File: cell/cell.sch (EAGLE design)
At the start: 11 parts

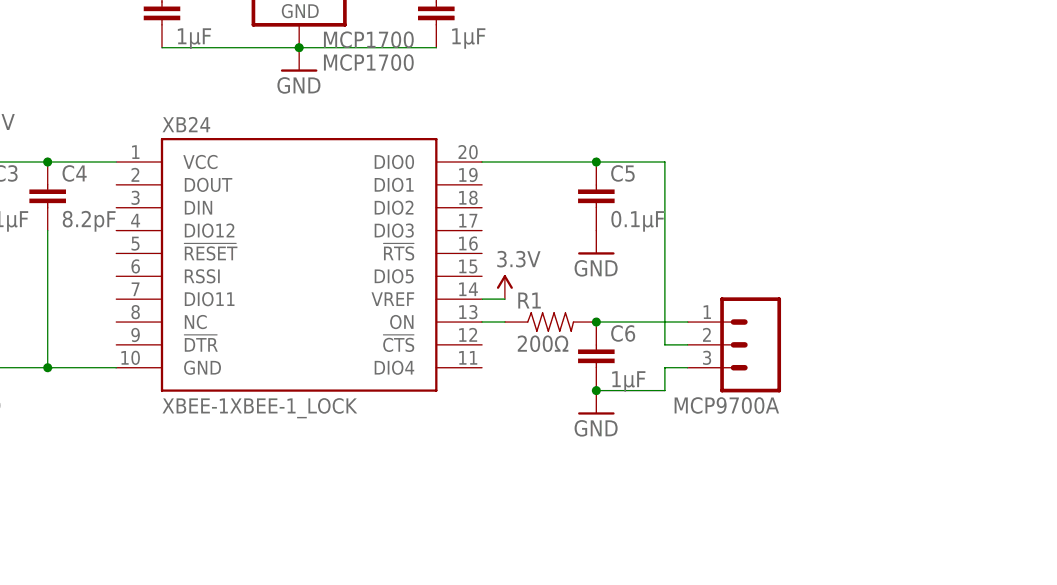
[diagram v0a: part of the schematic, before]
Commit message: cell v0.2, with on-board temperature sensor and better layout
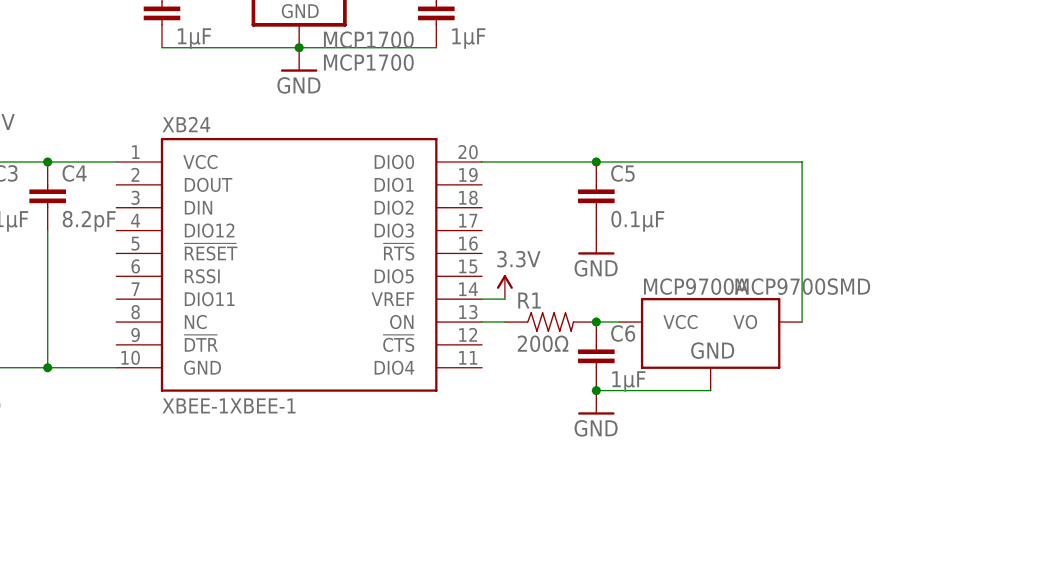
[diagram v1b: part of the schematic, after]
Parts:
- MCP9700A: value (none) -> MCP9700SMD; device SparkFun-Connectors:M03LOCK -> SparkFun-Sensors:MCP9700SMD
- XB24: value XBEE-1XBEE-1_LOCK -> XBEE-1XBEE-1; device hrldcpr:XBEE-1XBEE-1_LOCK -> hrldcpr:XBEE-1XBEE-1
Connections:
- net GND: now also MCP9700A.GND; no longer MCP9700A.3
- net N$1: now also MCP9700A.VCC; no longer MCP9700A.1
- net N$3: now also MCP9700A.VO; no longer MCP9700A.2
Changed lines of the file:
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@@
 <part name="C6" library="SparkFun-Capacitors" deviceset="CAP" device="0805" value="1µF"/>
 <part name="R1" library="SparkFun-Resistors" deviceset="RESISTOR" device="0805-RES" value="200Ω"/>
-<part name="XB24" library="hrldcpr" deviceset="XBEE-1" device="XBEE-1_LOCK"/>
 <part name="MCP1700" library="hrldcpr" deviceset="MCP1700" device=""/>
 <part name="C2" library="SparkFun-Capacitors" deviceset="CAP" device="0805" value="1µF"/>
-<part name="MCP9700A" library="SparkFun-Connectors" deviceset="M03" device="LOCK"/>
+<part name="MCP9700A" library="SparkFun-Sensors" deviceset="MCP9700" device="SMD"/>
+<part name="XB24" library="hrldcpr" deviceset="XBEE-1" device="XBEE-1"/>
 </parts>
 <sheets>
@@
 <instance part="C6" gate="G$1" x="137.16" y="76.2"/>
 <instance part="R1" gate="G$1" x="132.08" y="81.28"/>
-<instance part="XB24" gate="G$1" x="104.14" y="88.9"/>
 <instance part="MCP1700" gate="G$1" x="104.14" y="119.38"/>
 <instance part="C2" gate="G$1" x="119.38" y="114.3"/>
-<instance part="MCP9700A" gate="G$1" x="154.94" y="78.74" rot="R180"/>
+<instance part="MCP9700A" gate="G$1" x="149.86" y="78.74"/>
+<instance part="XB24" gate="G$1" x="104.14" y="88.9"/>
 </instances>
 <busses>
@@
 <pinref part="C6" gate="G$1" pin="2"/>
 <pinref part="C6" gate="G$1" pin="2"/>
-<wire x1="144.78" y1="76.2" x2="144.78" y2="73.66" width="0.1524" layer="91"/>
-<wire x1="144.78" y1="73.66" x2="137.16" y2="73.66" width="0.1524" layer="91"/>
 <junction x="137.16" y="73.66"/>
-<pinref part="MCP9700A" gate="G$1" pin="3"/>
-<wire x1="144.78" y1="76.2" x2="147.32" y2="76.2" width="0.1524" layer="91"/>
+<pinref part="MCP9700A" gate="G$1" pin="GND"/>
+<wire x1="137.16" y1="73.66" x2="149.86" y2="73.66" width="0.1524" layer="91"/>
 </segment>
 <segment>
@@
 <pinref part="C6" gate="G$1" pin="1"/>
 <pinref part="R1" gate="G$1" pin="2"/>
-<wire x1="147.32" y1="81.28" x2="137.16" y2="81.28" width="0.1524" layer="91"/>
+<pinref part="MCP9700A" gate="G$1" pin="VCC"/>
+<pinref part="MCP9700A" gate="G$1" pin="VCC"/>
+<wire x1="139.7" y1="81.28" x2="137.16" y2="81.28" width="0.1524" layer="91"/>
 <junction x="137.16" y="81.28"/>
-<pinref part="MCP9700A" gate="G$1" pin="1"/>
 </segment>
 </net>
@@
 <pinref part="C5" gate="G$1" pin="1"/>
 <wire x1="137.16" y1="99.06" x2="124.46" y2="99.06" width="0.1524" layer="91"/>
-<wire x1="137.16" y1="99.06" x2="144.78" y2="99.06" width="0.1524" layer="91"/>
-<wire x1="144.78" y1="99.06" x2="144.78" y2="78.74" width="0.1524" layer="91"/>
 <junction x="137.16" y="99.06"/>
+<pinref part="MCP9700A" gate="G$1" pin="VO"/>
+<wire x1="160.02" y1="81.28" x2="160.02" y2="99.06" width="0.1524" layer="91"/>
+<wire x1="160.02" y1="99.06" x2="137.16" y2="99.06" width="0.1524" layer="91"/>
 <pinref part="XB24" gate="G$1" pin="DIO0"/>
-<pinref part="MCP9700A" gate="G$1" pin="2"/>
-<wire x1="144.78" y1="78.74" x2="147.32" y2="78.74" width="0.1524" layer="91"/>
 </segment>
 </net>

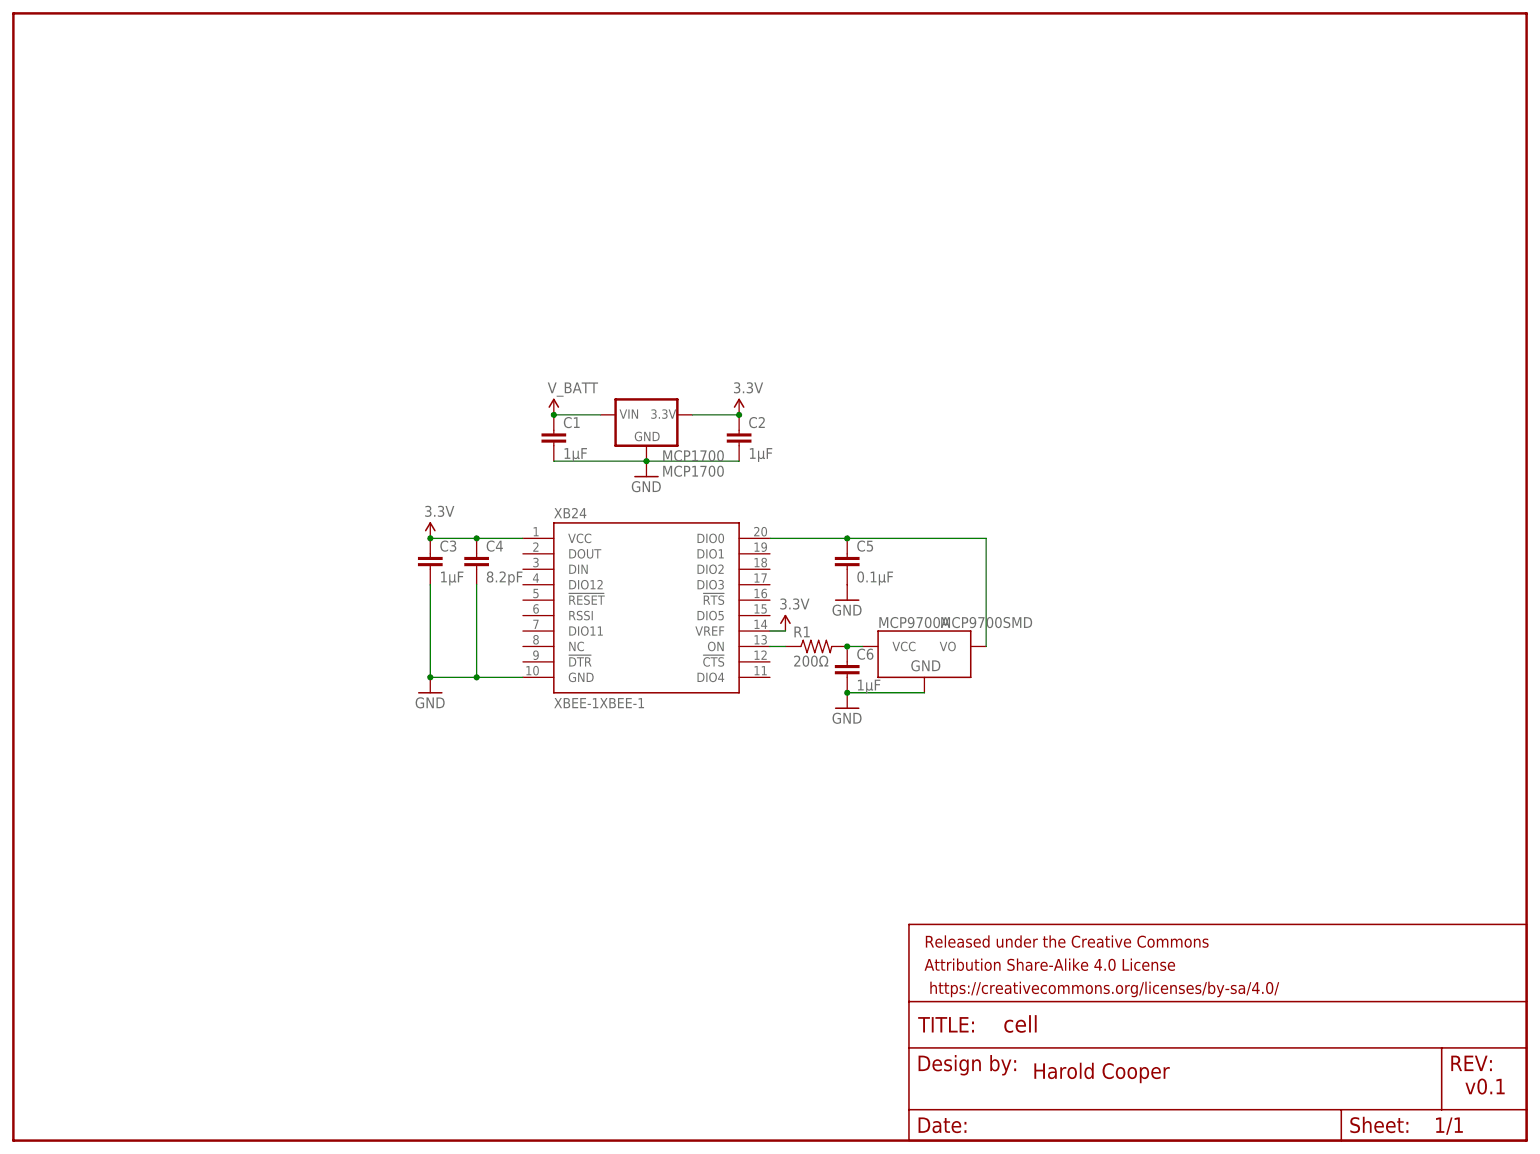
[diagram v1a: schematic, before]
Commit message: ground DIN/!CONFIG so that we can safely disable its pullup resistor
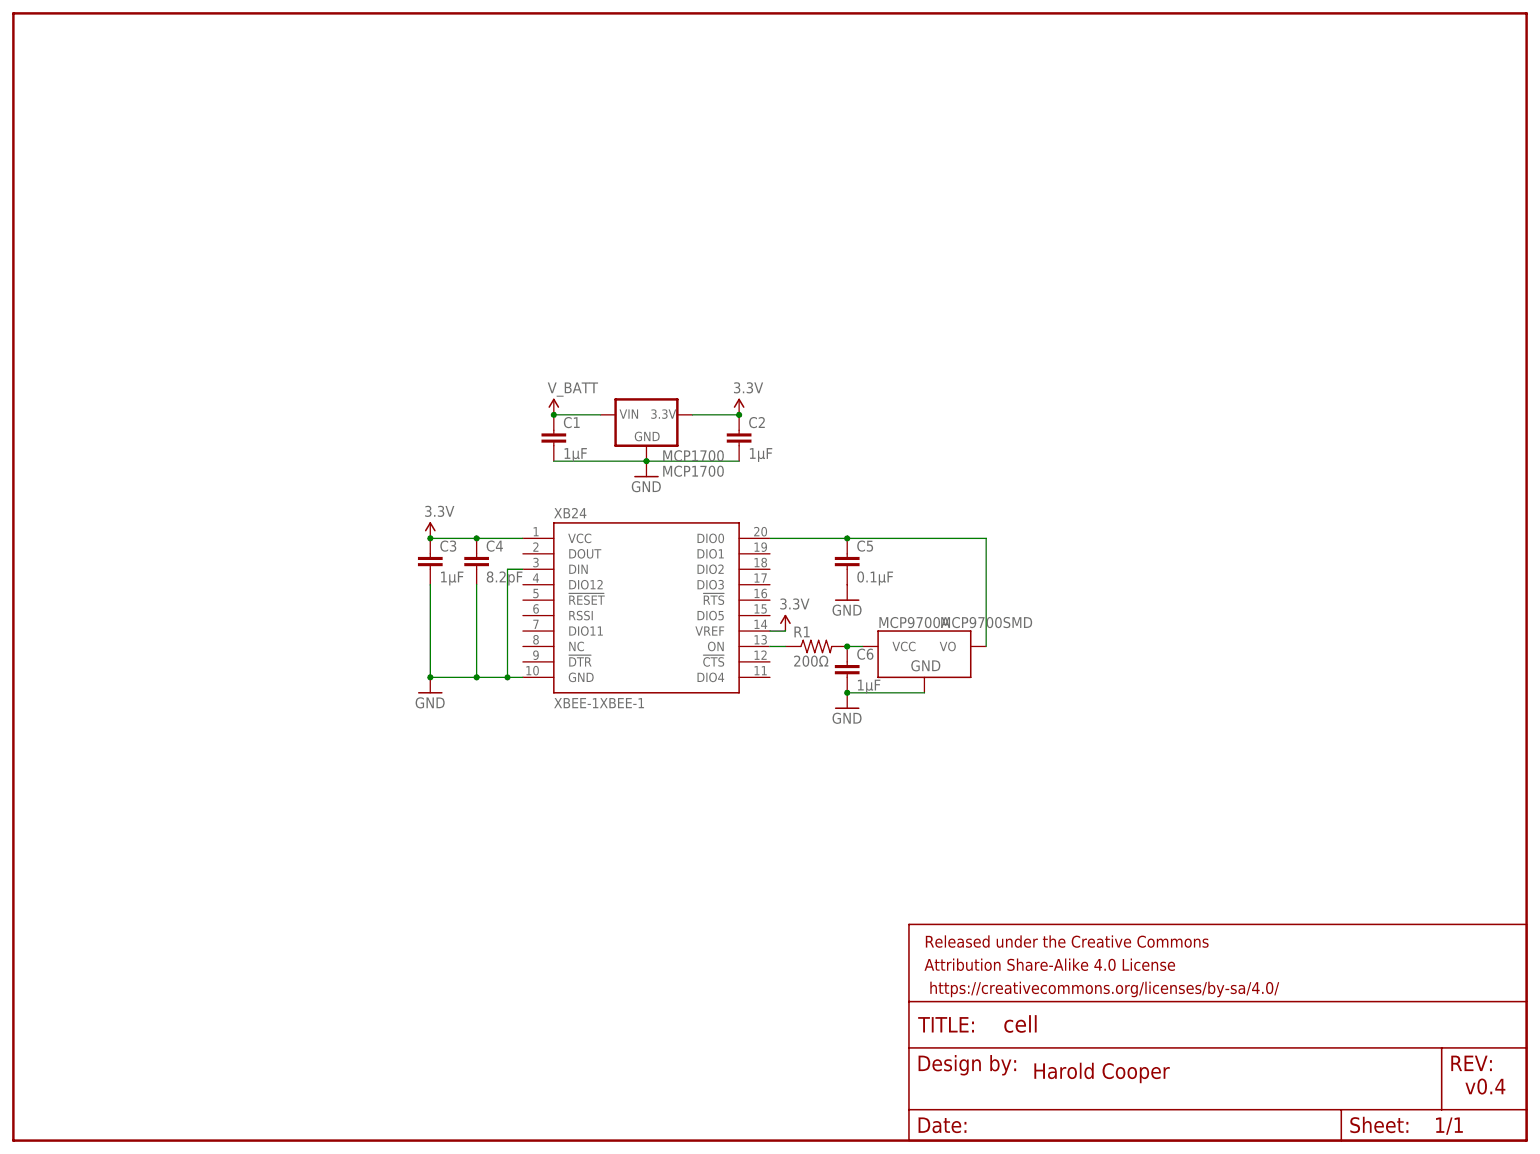
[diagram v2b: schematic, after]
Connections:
- net GND: now also XB24.DIN
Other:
- note added: "v0.4"
- note removed: "v0.1"
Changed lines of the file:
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@@
 <plain>
 <text x="167.64" y="10.16" size="2.54" layer="94">Harold Cooper</text>
-<text x="238.76" y="7.62" size="2.54" layer="94">v0.1</text>
+<text x="238.76" y="7.62" size="2.54" layer="94">v0.4</text>
 </plain>
 <instances>
@@
 <pinref part="GND2" gate="1" pin="GND"/>
 <wire x1="68.58" y1="91.44" x2="68.58" y2="76.2" width="0.1524" layer="91"/>
-<wire x1="83.82" y1="76.2" x2="76.2" y2="76.2" width="0.1524" layer="91"/>
+<wire x1="83.82" y1="76.2" x2="81.28" y2="76.2" width="0.1524" layer="91"/>
 <junction x="68.58" y="76.2"/>
 <pinref part="C4" gate="G$1" pin="2"/>
+<wire x1="81.28" y1="76.2" x2="76.2" y2="76.2" width="0.1524" layer="91"/>
 <wire x1="76.2" y1="76.2" x2="68.58" y2="76.2" width="0.1524" layer="91"/>
 <wire x1="76.2" y1="91.44" x2="76.2" y2="76.2" width="0.1524" layer="91"/>
 <junction x="76.2" y="76.2"/>
 <pinref part="XB24" gate="G$1" pin="GND"/>
+<pinref part="XB24" gate="G$1" pin="DIN"/>
+<wire x1="83.82" y1="93.98" x2="81.28" y2="93.98" width="0.1524" layer="91"/>
+<wire x1="81.28" y1="93.98" x2="81.28" y2="76.2" width="0.1524" layer="91"/>
+<junction x="81.28" y="76.2"/>
 </segment>
 </net>
